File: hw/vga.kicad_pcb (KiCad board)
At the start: 2 copper layers, 36.8 x 36.8 mm, 19 parts, among them J1 Conn_02x05_Odd_Even, J2 DB15_Female_HighDensity_Mount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, U1 74HC4053, U2 23LCV512, U3 ICS501

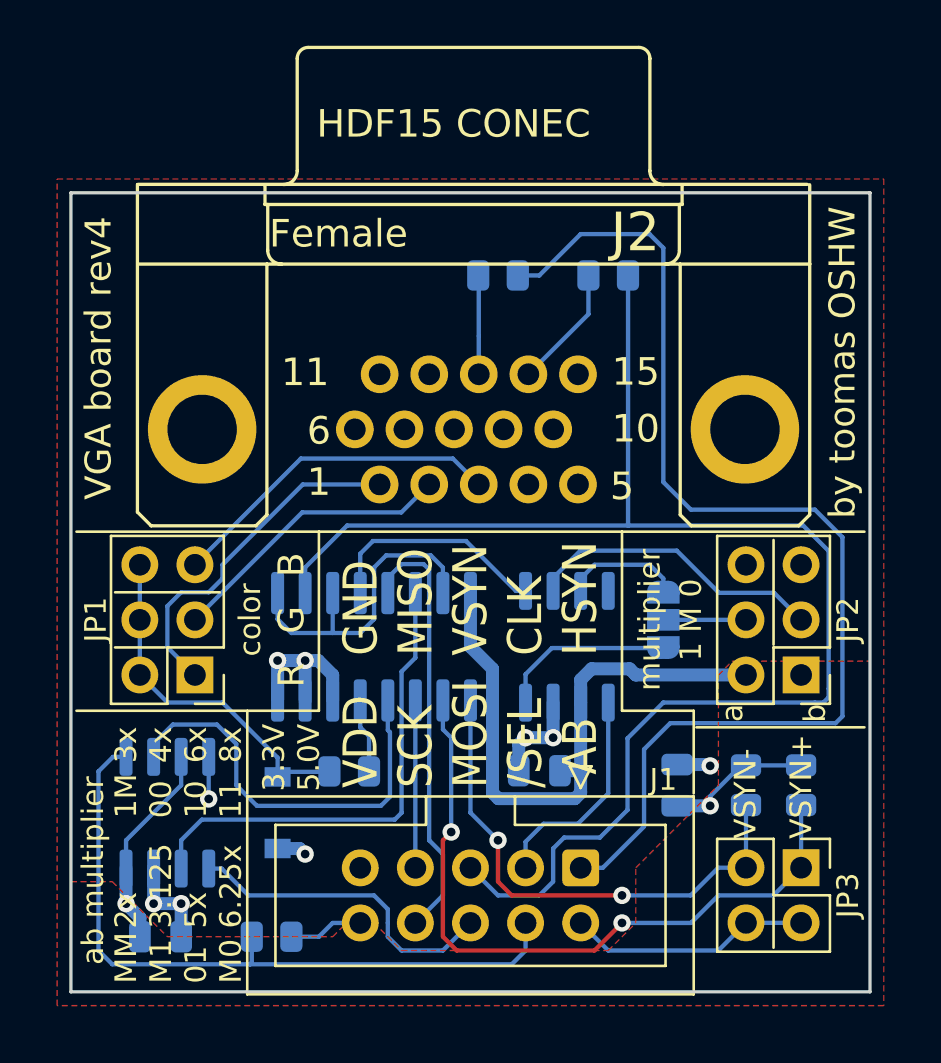
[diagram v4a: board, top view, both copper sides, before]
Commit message: Cleaned up the schematic and changed some resistor values for better impedance matching
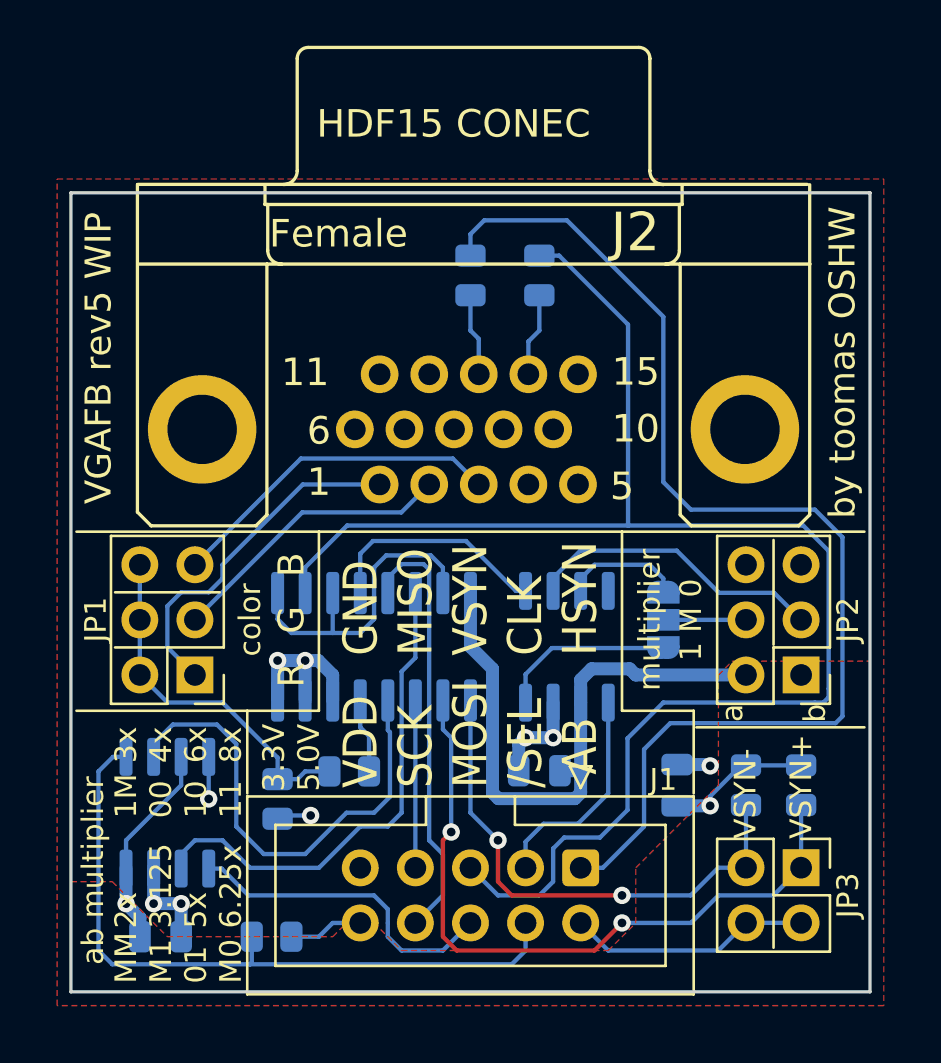
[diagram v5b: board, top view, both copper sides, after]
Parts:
- removed D1: 1N4148, Diode_SMD:D_SOD-123
- added R7: 100, Resistor_SMD:R_0805_2012Metric, B.Cu at (143.5, 94.6)
- R4, R5: value 68 -> 22
- R6: value 470 -> 220
- moved R5 3.18 mm to (155.6, 70.5), turned to 90 degrees
- moved R4 1.27 mm to (152.4, 70.5), turned to 90 degrees
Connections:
- net /HSYNC_OUT renamed Net-(J2-Pad13)
- net /VSYNC_OUT renamed Net-(J2-Pad14)
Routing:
- net /VSYNC: track 68.5 -> 71.7 mm
- net Net-(U1-Pad4): track 19.2 -> 22.1 mm
- net Net-(J2-Pad14): track 5.70 -> 3.85 mm
- net /HSYNC: track 53.2 -> 54.2 mm
- net Net-(J2-Pad13): track 4.57 -> 3.80 mm
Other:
- board text added: "VGAFB rev5 WIP"
- board text added: "github.com/tlaasik/vgafb"
- board text removed: "VGA board rev4"
- board text removed: "https://hithub.com/tlaasik/vgafb"
